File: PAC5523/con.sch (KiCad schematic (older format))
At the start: 38 parts

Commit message: updated schematic
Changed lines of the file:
@@
 Wire Wire Line
 	6950 1450 7050 1450
-Text GLabel 7050 1450 1    50   Input ~ 0
-VIO
 $Comp
 L Device:R_Small R?
@@
 	1    0    0    -1
 $EndComp
+$Comp
+L power:+5V #PWR?
+U 1 1 5D60DF02
+P 7050 1450
+F 0 "#PWR?" H 7050 1300 50  0001 C CNN
+F 1 "+5V" H 7065 1623 50  0000 C CNN
+F 2 "" H 7050 1450 50  0001 C CNN
+F 3 "" H 7050 1450 50  0001 C CNN
+	1    7050 1450
+	1    0    0    -1
+$EndComp
+Connection ~ 7050 1450
 $EndSCHEMATC

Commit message: updated schematic
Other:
- note added: "NTC Spannungsteiler fixen\n"
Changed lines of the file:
@@
 $EndComp
 Connection ~ 7050 1450
+Text Notes 8050 4150 0    50   ~ 0
+NTC Spannungsteiler fixen\n
 $EndSCHEMATC

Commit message: wip
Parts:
- removed J?: CAN, Connector_Molex:Molex_PicoBlade_53261-0371_1x03-1MP_P1.25mm_Horizontal, symbol Connector_Generic_MountingPin:Conn_01x03_MountingPin
- removed JP? (x2): UART/RS485, Jumper:SolderJumper-3_P1.3mm_Bridged2Bar12_Pad1.0x1.5mm, symbol Jumper:Jumper_3_Bridged12
- added J4: GND, otter:PinHeader_1x03_P2.00mm_Vertical_COMBI, symbol Connector:Conn_01x03_Male
- added J5: VIN, otter:PinHeader_1x03_P2.00mm_Vertical_COMBI, symbol Connector:Conn_01x03_Male
- added R43: 100, Resistor_SMD:R_0603_1608Metric, symbol Device:R_Small
- added R44: 1k, Resistor_SMD:R_0603_1608Metric, symbol Device:R_Small
- JP2, JP4: renamed from JP?; footprint Jumper:SolderJumper-3_P1.3mm_Bridged2Bar12_Pad1.0x1.5mm -> Jumper:SolderJumper-3_P1.3mm_Open_Pad1.0x1.5mm_NumberLabels
- gave numbers to parts that had none: 33
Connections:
- net labels added: NTC_EXT, VIN
- wire segments 31 -> 27
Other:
- note removed: "NTC Spannungsteiler fixen\n"
- moved on the sheet: JP2, R32, R39, R4, R5

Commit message: wip
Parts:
- removed JP4: HALL_V, Jumper:SolderJumper-3_P1.3mm_Open_Pad1.0x1.5mm_NumberLabels, symbol Jumper:Jumper_3_Bridged12
- removed R20: 120, Resistor_SMD:R_0603_1608Metric, symbol Device:R_Small
- removed R37: 1k, Resistor_SMD:R_0603_1608Metric, symbol Device:R_Small
- removed R38: 100, Resistor_SMD:R_0603_1608Metric, symbol Device:R_Small
- added J9: LED, Connector_Molex:Molex_PicoBlade_53261-0371_1x03-1MP_P1.25mm_Horizontal, symbol Connector_Generic_MountingPin:Conn_01x03_MountingPin
- added R45: 100, Resistor_SMD:R_0603_1608Metric, symbol Device:R_Small
- added R46, R47: 1k, Resistor_SMD:R_0603_1608Metric, symbol Device:R_Small
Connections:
- net labels added: 3V3, AIN, CANRX, CANTX
- net labels removed: NTC_FET, NTC_FET_PAC, UART_RX, UART_TX
- wire segments 27 -> 35
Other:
- moved on the sheet: R27, R28, R29, R33, R34, R35

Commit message: wip
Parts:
- removed J7: SWD, Connector_PinHeader_2.54mm:PinHeader_1x04_P2.54mm_Vertical, symbol Connector:Conn_01x04_Male
- removed R21, R22: 100, Resistor_SMD:R_0603_1608Metric, symbol Device:R_Small
- added P1: TC2030-CTX-Tag-Connect, otter:TC2030, symbol otter:TC2030-CTX-Tag-Connect
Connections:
- no-connect marks 0 -> 2
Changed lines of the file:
@@
 Wire Wire Line
 	3150 3500 3100 3500
-$Comp
-L Connector:Conn_01x04_Male J?
-U 1 1 5D5B75A0
-P 4900 3450
-AR Path="/5D5B75A0" Ref="J?"  Part="1"
-AR Path="/5D59ABFE/5D5B75A0" Ref="J7"  Part="1"
-F 0 "J7" H 4872 3332 50  0000 R CNN
-F 1 "SWD" H 4872 3423 50  0000 R CNN
-F 2 "Connector_PinHeader_2.54mm:PinHeader_1x04_P2.54mm_Vertical" H 4900 3450 50  0001 C CNN
-F 3 "~" H 4900 3450 50  0001 C CNN
-	1    4900 3450
-	-1   0    0    1
-$EndComp
-Text GLabel 4700 3250 1    50   Input ~ 0
-VIO
-$Comp
-L power:GND #PWR?
-U 1 1 5D5B75A7
-P 4700 3550
-AR Path="/5D5B75A7" Ref="#PWR?"  Part="1"
-AR Path="/5D59ABFE/5D5B75A7" Ref="#PWR0138"  Part="1"
-F 0 "#PWR0138" H 4700 3300 50  0001 C CNN
-F 1 "GND" H 4705 3377 50  0000 C CNN
-F 2 "" H 4700 3550 50  0001 C CNN
-F 3 "" H 4700 3550 50  0001 C CNN
-	1    4700 3550
-	1    0    0    -1
-$EndComp
 Text GLabel 2350 3600 1    50   Input ~ 0
 RS485_A
@@
 	0    1    1    0
 $EndComp
-$Comp
-L Device:R_Small R?
-U 1 1 5D5B75DF
-P 4600 3350
-AR Path="/5D5B75DF" Ref="R?"  Part="1"
-AR Path="/5D59ABFE/5D5B75DF" Ref="R21"  Part="1"
-F 0 "R21" V 4400 3300 50  0000 C CNN
-F 1 "100" V 4500 3300 50  0000 C CNN
-F 2 "Resistor_SMD:R_0603_1608Metric" H 4600 3350 50  0001 C CNN
-F 3 "~" H 4600 3350 50  0001 C CNN
-	1    4600 3350
-	0    1    1    0
-$EndComp
-$Comp
-L Device:R_Small R?
-U 1 1 5D5B75E5
-P 4600 3450
-AR Path="/5D5B75E5" Ref="R?"  Part="1"
-AR Path="/5D59ABFE/5D5B75E5" Ref="R22"  Part="1"
-F 0 "R22" V 4704 3450 50  0000 C CNN
-F 1 "100" V 4795 3450 50  0000 C CNN
-F 2 "Resistor_SMD:R_0603_1608Metric" H 4600 3450 50  0001 C CNN
-F 3 "~" H 4600 3450 50  0001 C CNN
-	1    4600 3450
-	0    1    1    0
-$EndComp
-Text GLabel 4500 3450 0    50   Input ~ 0
-SWDCL
-Text GLabel 4500 3350 0    50   Input ~ 0
-SWDIO
 $Comp
 L power:GND #PWR?
@@
 	5850 3600 6100 3600
 Connection ~ 6100 3600
+$Comp
+L otter:TC2030-CTX-Tag-Connect P?
+U 1 1 5CD67ED4
+P 7800 2500
+AR Path="/5CD67ED4" Ref="P?"  Part="1"
+AR Path="/5D59ABFE/5CD67ED4" Ref="P1"  Part="1"
+F 0 "P1" H 7800 2792 40  0000 C CNN
+F 1 "TC2030-CTX-Tag-Connect" H 7800 2716 40  0000 C CNN
+F 2 "otter:TC2030" H 7800 2500 60  0001 C CNN
+F 3 "" H 7800 2500 60  0001 C CNN
+	1    7800 2500
+	1    0    0    -1
+$EndComp
+Text GLabel 7350 2400 0    50   Input ~ 0
+VIO
+$Comp
+L power:GND #PWR?
+U 1 1 5CD67EDB
+P 7350 2600
+AR Path="/5CD67EDB" Ref="#PWR?"  Part="1"
+AR Path="/5D59ABFE/5CD67EDB" Ref="#PWR0133"  Part="1"
+F 0 "#PWR0133" H 7350 2350 50  0001 C CNN
+F 1 "GND" V 7355 2472 50  0000 R CNN
+F 2 "" H 7350 2600 50  0001 C CNN
+F 3 "" H 7350 2600 50  0001 C CNN
+	1    7350 2600
+	0    1    1    0
+$EndComp
+Text GLabel 8250 2500 2    50   Input ~ 0
+SWDCL
+Text GLabel 8250 2400 2    50   Input ~ 0
+SWDIO
+NoConn ~ 8250 2600
+NoConn ~ 7350 2500
 $EndSCHEMATC

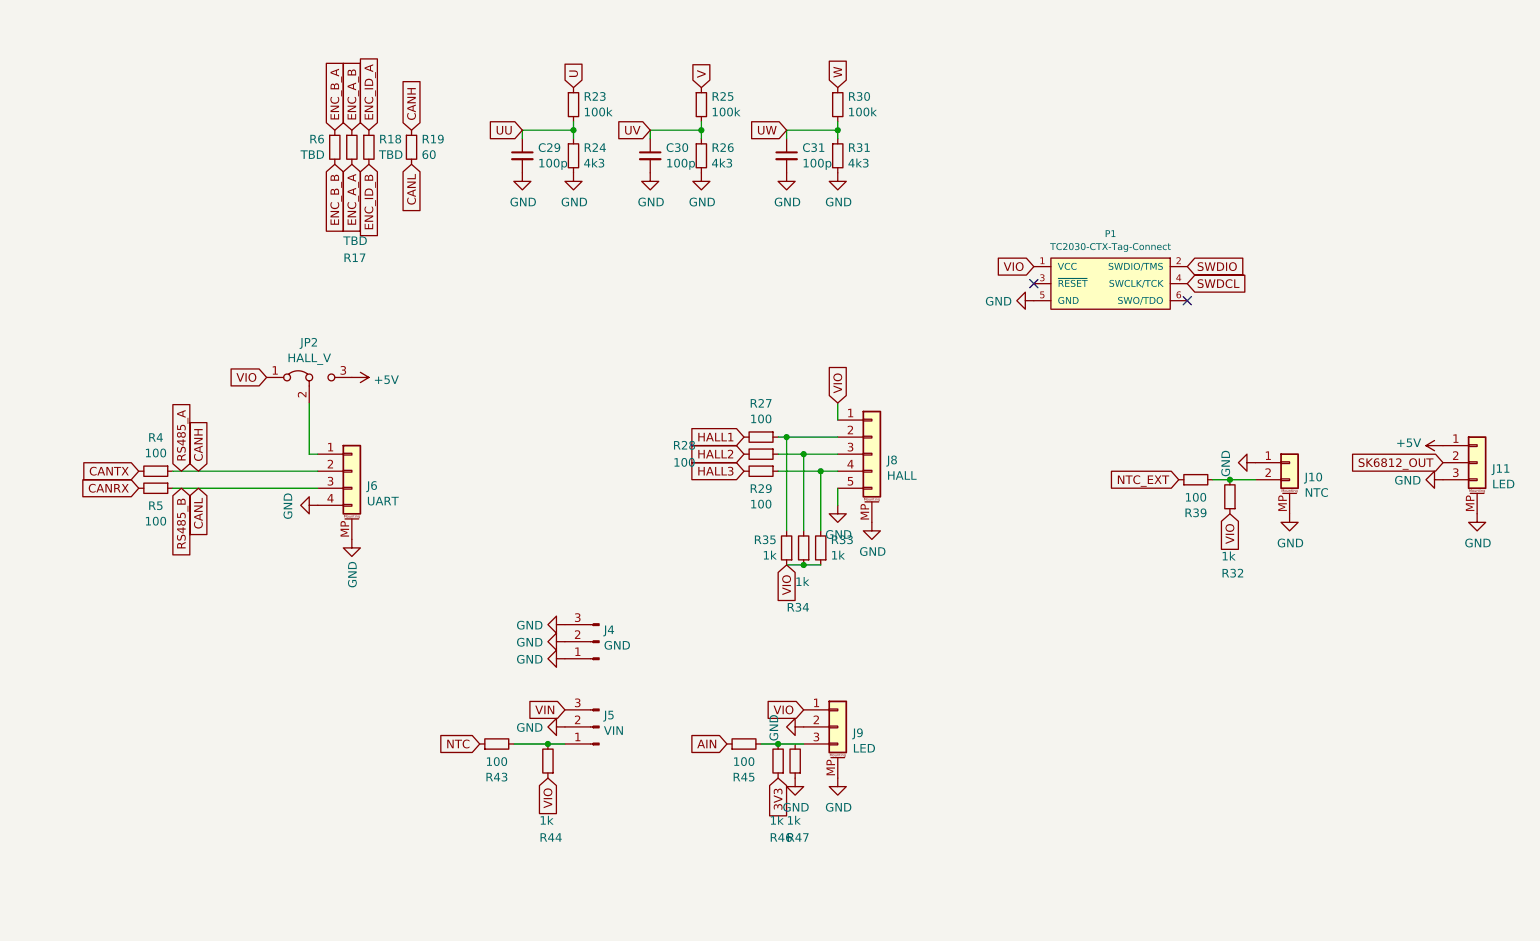
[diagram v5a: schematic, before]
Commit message: added Encoder,LED,NTC
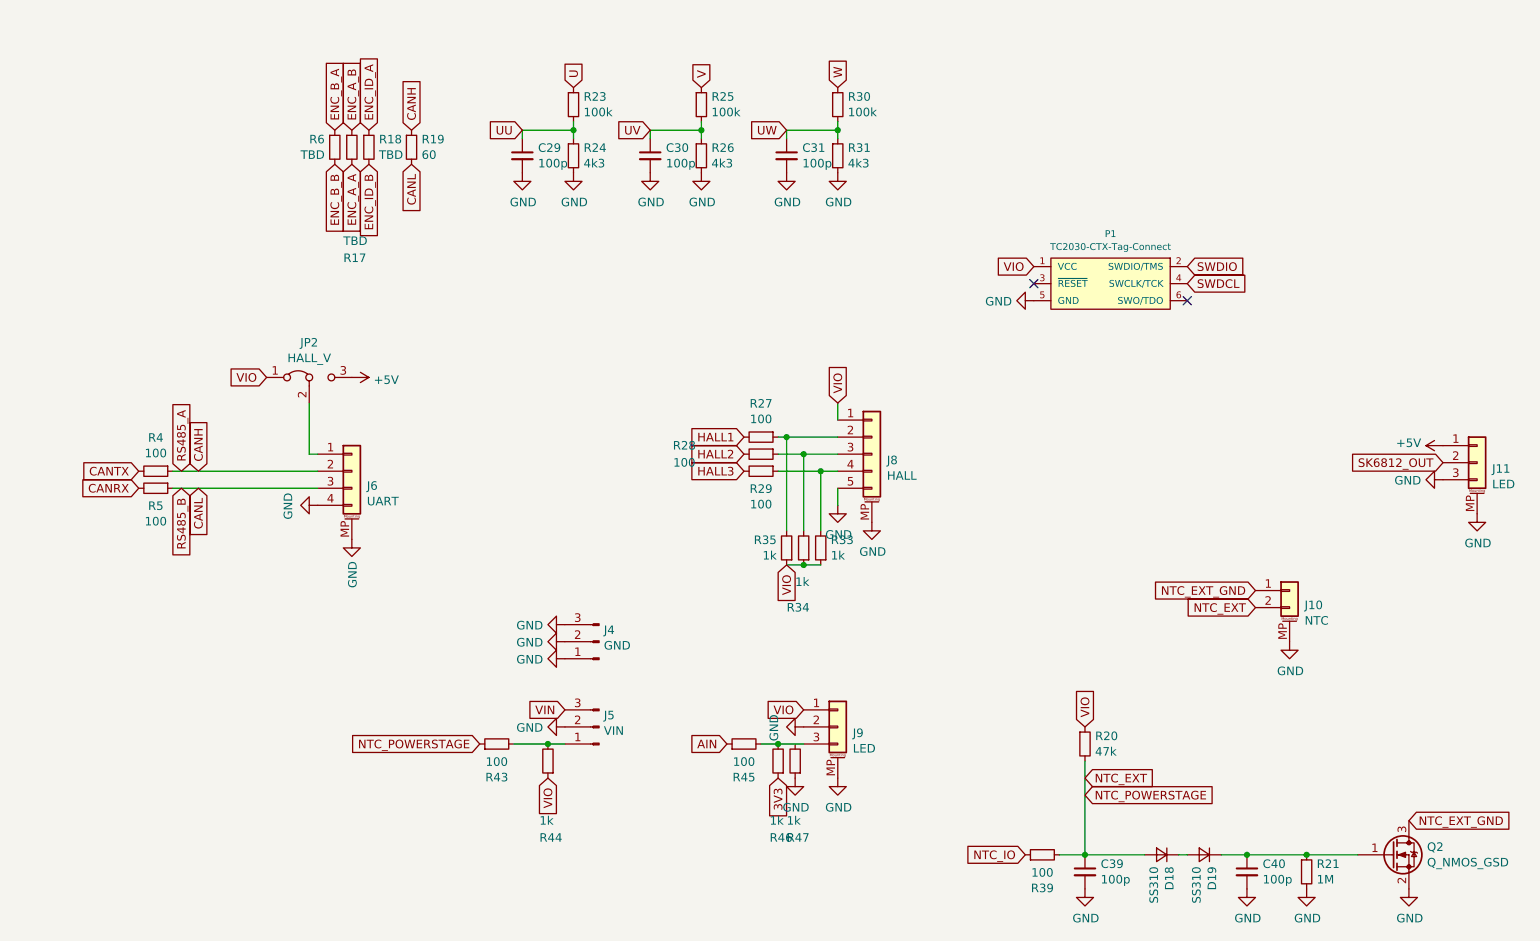
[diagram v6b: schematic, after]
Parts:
- removed R32: 1k, Resistor_SMD:R_0603_1608Metric, symbol Device:R_Small
- added C39, C40: 100p, Capacitor_SMD:C_0603_1608Metric, symbol Device:C_Small
- added D18, D19: SS310, Diode_SMD:D_SOD-123F, symbol Device:D_Small
- added Q2: Q_NMOS_GSD, Package_TO_SOT_SMD:SOT-23, symbol Device:Q_NMOS_GSD
- added R20: 47k, Resistor_SMD:R_0603_1608Metric, symbol Device:R_Small
- added R21: 1M, Resistor_SMD:R_0603_1608Metric, symbol Device:R_Small
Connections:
- net NTC is gone; now on net NTC_EXT: R43.1
- net GND: now also C39.2, C40.2, Q2.2 (S), R21.2; no longer J10.1 (Pin_1)
- net NTC_EXT: now also J10.2 (Pin_2), R39.2, C39.1, D18.2 (A), R20.2; no longer R39.1
- net VIO: now also R20.1
- new net: C40.1, D19.1 (K), Q2.1 (G), R21.1
- new net: D18.1 (K), D19.2 (A)
- new net NTC_EXT_GND: J10.1 (Pin_1), Q2.3 (D)
- new net NTC_IO: R39.1
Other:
- moved on the sheet: J10, R39
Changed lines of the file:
@@
 L Device:R_Small R?
 U 1 1 5D5B7552
-P 8300 3650
+P 7400 5850
 AR Path="/5D5B7552" Ref="R?"  Part="1"
 AR Path="/5D59ABFE/5D5B7552" Ref="R39"  Part="1"
-F 0 "R39" V 8104 3650 50  0000 C CNN
-F 1 "100" V 8195 3650 50  0000 C CNN
-F 2 "Resistor_SMD:R_0603_1608Metric" H 8300 3650 50  0001 C CNN
-F 3 "~" H 8300 3650 50  0001 C CNN
-	1    8300 3650
+F 0 "R39" V 7204 5850 50  0000 C CNN
+F 1 "100" V 7295 5850 50  0000 C CNN
+F 2 "Resistor_SMD:R_0603_1608Metric" H 7400 5850 50  0001 C CNN
+F 3 "~" H 7400 5850 50  0001 C CNN
+	1    7400 5850
 	0    -1   -1   0
 $EndComp
-Text GLabel 8200 3650 0    50   Input ~ 0
+Text GLabel 8650 4400 0    50   Input ~ 0
 NTC_EXT
 Text GLabel 2450 3700 3    50   Input ~ 0
@@
 L Connector_Generic_MountingPin:Conn_01x02_MountingPin J?
 U 1 1 5D5B75FF
-P 8850 3550
+P 8850 4300
 AR Path="/5D5B75FF" Ref="J?"  Part="1"
 AR Path="/5D59ABFE/5D5B75FF" Ref="J10"  Part="1"
-F 0 "J10" H 8938 3464 50  0000 L CNN
-F 1 "NTC" H 8938 3373 50  0000 L CNN
-F 2 "Connector_Molex:Molex_PicoBlade_53261-0271_1x02-1MP_P1.25mm_Horizontal" H 8850 3550 50  0001 C CNN
-F 3 "~" H 8850 3550 50  0001 C CNN
-	1    8850 3550
+F 0 "J10" H 8938 4214 50  0000 L CNN
+F 1 "NTC" H 8938 4123 50  0000 L CNN
+F 2 "Connector_Molex:Molex_PicoBlade_53261-0271_1x02-1MP_P1.25mm_Horizontal" H 8850 4300 50  0001 C CNN
+F 3 "~" H 8850 4300 50  0001 C CNN
+	1    8850 4300
 	1    0    0    -1
 $EndComp
@@
 L power:GND #PWR?
 U 1 1 5D5B7605
-P 8850 3850
+P 8850 4600
 AR Path="/5D5B7605" Ref="#PWR?"  Part="1"
 AR Path="/5D59ABFE/5D5B7605" Ref="#PWR0143"  Part="1"
-F 0 "#PWR0143" H 8850 3600 50  0001 C CNN
-F 1 "GND" H 8855 3677 50  0000 C CNN
-F 2 "" H 8850 3850 50  0001 C CNN
-F 3 "" H 8850 3850 50  0001 C CNN
-	1    8850 3850
-	1    0    0    -1
-$EndComp
-$Comp
-L power:GND #PWR?
-U 1 1 5D5B760B
-P 8650 3550
-AR Path="/5D5B760B" Ref="#PWR?"  Part="1"
-AR Path="/5D59ABFE/5D5B760B" Ref="#PWR0145"  Part="1"
-F 0 "#PWR0145" H 8650 3300 50  0001 C CNN
-F 1 "GND" H 8655 3377 50  0000 C CNN
-F 2 "" H 8650 3550 50  0001 C CNN
-F 3 "" H 8650 3550 50  0001 C CNN
-	1    8650 3550
-	0    1    1    0
+F 0 "#PWR0143" H 8850 4350 50  0001 C CNN
+F 1 "GND" H 8855 4427 50  0000 C CNN
+F 2 "" H 8850 4600 50  0001 C CNN
+F 3 "" H 8850 4600 50  0001 C CNN
+	1    8850 4600
+	1    0    0    -1
 $EndComp
 $Comp
@@
 $EndComp
 Text GLabel 4100 5200 0    50   Input ~ 0
-NTC
+NTC_POWERSTAGE
 Wire Wire Line
 	4300 5200 4500 5200
@@
 	-1   0    0    1
 $EndComp
-Text GLabel 8500 3850 3    50   Input ~ 0
-VIO
-$Comp
-L Device:R_Small R?
-U 1 1 5D5B7514
-P 8500 3750
-AR Path="/5D5B7514" Ref="R?"  Part="1"
-AR Path="/5D59ABFE/5D5B7514" Ref="R32"  Part="1"
-F 0 "R32" H 8550 4200 50  0000 R CNN
-F 1 "1k" H 8550 4100 50  0000 R CNN
-F 2 "Resistor_SMD:R_0603_1608Metric" H 8500 3750 50  0001 C CNN
-F 3 "~" H 8500 3750 50  0001 C CNN
-	1    8500 3750
-	-1   0    0    1
-$EndComp
 Connection ~ 4500 5200
 Wire Wire Line
 	4500 5200 4600 5200
-Wire Wire Line
-	8400 3650 8500 3650
-Connection ~ 8500 3650
-Wire Wire Line
-	8500 3650 8650 3650
 $Comp
 L Device:R_Small R?
@@
 NoConn ~ 8250 2600
 NoConn ~ 7350 2500
+Text GLabel 7650 5400 2    50   Input ~ 0
+NTC_EXT
+Text GLabel 7650 5500 2    50   Input ~ 0
+NTC_POWERSTAGE
+Text GLabel 7300 5850 0    50   Input ~ 0
+NTC_IO
+$Comp
+L Device:R_Small R?
+U 1 1 5CDE0535
+P 8950 5950
+AR Path="/5CDE0535" Ref="R?"  Part="1"
+AR Path="/5D59ABFE/5CDE0535" Ref="R21"  Part="1"
+F 0 "R21" H 9009 5996 50  0000 L CNN
+F 1 "1M" H 9009 5905 50  0000 L CNN
+F 2 "Resistor_SMD:R_0603_1608Metric" H 8950 5950 50  0001 C CNN
+F 3 "~" H 8950 5950 50  0001 C CNN
+	1    8950 5950
+	1    0    0    -1
+$EndComp
+$Comp
+L Device:C_Small C?
+U 1 1 5CDE053B
+P 7650 5950
+AR Path="/5CDE053B" Ref="C?"  Part="1"
+AR Path="/5D59ABFE/5CDE053B" Ref="C39"  Part="1"
+F 0 "C39" H 7742 5996 50  0000 L CNN
+F 1 "100p" H 7742 5905 50  0000 L CNN
+F 2 "Capacitor_SMD:C_0603_1608Metric" H 7650 5950 50  0001 C CNN
+F 3 "~" H 7650 5950 50  0001 C CNN
+	1    7650 5950
+	1    0    0    -1
+$EndComp
+$Comp
+L Device:D_Small D?
+U 1 1 5CDE1DA1
+P 8100 5850
+AR Path="/5CDE1DA1" Ref="D?"  Part="1"
+AR Path="/5D59ABFE/5CDE1DA1" Ref="D18"  Part="1"
+F 0 "D18" V 8054 5918 50  0000 L CNN
+F 1 "SS310" V 8145 5918 50  0000 L CNN
+F 2 "Diode_SMD:D_SOD-123F" V 8100 5850 50  0001 C CNN
+F 3 "~" V 8100 5850 50  0001 C CNN
+	1    8100 5850
+	-1   0    0    1
+$EndComp
+$Comp
+L Device:D_Small D?
+U 1 1 5CDE236C
+P 8350 5850
+AR Path="/5CDE236C" Ref="D?"  Part="1"
+AR Path="/5D59ABFE/5CDE236C" Ref="D19"  Part="1"
+F 0 "D19" V 8304 5918 50  0000 L CNN
+F 1 "SS310" V 8395 5918 50  0000 L CNN
+F 2 "Diode_SMD:D_SOD-123F" V 8350 5850 50  0001 C CNN
+F 3 "~" V 8350 5850 50  0001 C CNN
+	1    8350 5850
+	-1   0    0    1
+$EndComp
+$Comp
+L Device:C_Small C?
+U 1 1 5CDE366D
+P 8600 5950
+AR Path="/5CDE366D" Ref="C?"  Part="1"
+AR Path="/5D59ABFE/5CDE366D" Ref="C40"  Part="1"
+F 0 "C40" H 8692 5996 50  0000 L CNN
+F 1 "100p" H 8692 5905 50  0000 L CNN
+F 2 "Capacitor_SMD:C_0603_1608Metric" H 8600 5950 50  0001 C CNN
+F 3 "~" H 8600 5950 50  0001 C CNN
+	1    8600 5950
+	1    0    0    -1
+$EndComp
+Wire Wire Line
+	8000 5850 7650 5850
+Connection ~ 7650 5850
+Wire Wire Line
+	7650 5850 7500 5850
+Wire Wire Line
+	8950 5850 8600 5850
+Connection ~ 8600 5850
+Wire Wire Line
+	8600 5850 8450 5850
+Wire Wire Line
+	8250 5850 8200 5850
+$Comp
+L power:GND #PWR?
+U 1 1 5CDE791A
+P 8600 6050
+AR Path="/5CDE791A" Ref="#PWR?"  Part="1"
+AR Path="/5D59ABFE/5CDE791A" Ref="#PWR0138"  Part="1"
+F 0 "#PWR0138" H 8600 5800 50  0001 C CNN
+F 1 "GND" H 8605 5877 50  0000 C CNN
+F 2 "" H 8600 6050 50  0001 C CNN
+F 3 "" H 8600 6050 50  0001 C CNN
+	1    8600 6050
+	1    0    0    -1
+$EndComp
+$Comp
+L power:GND #PWR?
+U 1 1 5CDE80DA
+P 8950 6050
+AR Path="/5CDE80DA" Ref="#PWR?"  Part="1"
+AR Path="/5D59ABFE/5CDE80DA" Ref="#PWR0145"  Part="1"
+F 0 "#PWR0145" H 8950 5800 50  0001 C CNN
+F 1 "GND" H 8955 5877 50  0000 C CNN
+F 2 "" H 8950 6050 50  0001 C CNN
+F 3 "" H 8950 6050 50  0001 C CNN
+	1    8950 6050
+	1    0    0    -1
+$EndComp
+$Comp
+L power:GND #PWR?
+U 1 1 5CDE8848
+P 7650 6050
+AR Path="/5CDE8848" Ref="#PWR?"  Part="1"
+AR Path="/5D59ABFE/5CDE8848" Ref="#PWR0158"  Part="1"
+F 0 "#PWR0158" H 7650 5800 50  0001 C CNN
+F 1 "GND" H 7655 5877 50  0000 C CNN
+F 2 "" H 7650 6050 50  0001 C CNN
+F 3 "" H 7650 6050 50  0001 C CNN
+	1    7650 6050
+	1    0    0    -1
+$EndComp
+Wire Wire Line
+	8950 5850 9250 5850
+Connection ~ 8950 5850
+$Comp
+L Device:Q_NMOS_GSD Q2
+U 1 1 5CDECFF4
+P 9450 5850
+F 0 "Q2" H 9656 5896 50  0000 L CNN
+F 1 "Q_NMOS_GSD" H 9656 5805 50  0000 L CNN
+F 2 "Package_TO_SOT_SMD:SOT-23" H 9650 5950 50  0001 C CNN
+F 3 "~" H 9450 5850 50  0001 C CNN
+	1    9450 5850
+	1    0    0    -1
+$EndComp
+$Comp
+L power:GND #PWR0181
+U 1 1 5CDEE814
+P 9550 6050
+F 0 "#PWR0181" H 9550 5800 50  0001 C CNN
+F 1 "GND" H 9555 5877 50  0000 C CNN
+F 2 "" H 9550 6050 50  0001 C CNN
+F 3 "" H 9550 6050 50  0001 C CNN
+	1    9550 6050
+	1    0    0    -1
+$EndComp
+$Comp
+L Device:R_Small R?
+U 1 1 5CDEF71D
+P 7650 5200
+AR Path="/5CDEF71D" Ref="R?"  Part="1"
+AR Path="/5D59ABFE/5CDEF71D" Ref="R20"  Part="1"
+F 0 "R20" H 7709 5246 50  0000 L CNN
+F 1 "47k" H 7709 5155 50  0000 L CNN
+F 2 "Resistor_SMD:R_0603_1608Metric" H 7650 5200 50  0001 C CNN
+F 3 "~" H 7650 5200 50  0001 C CNN
+	1    7650 5200
+	1    0    0    -1
+$EndComp
+Text GLabel 7650 5100 1    50   Input ~ 0
+VIO
+Text GLabel 9550 5650 2    50   Input ~ 0
+NTC_EXT_GND
+Text GLabel 8650 4300 0    50   Input ~ 0
+NTC_EXT_GND
+Wire Wire Line
+	7650 5300 7650 5850
 $EndSCHEMATC

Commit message: placement almost done
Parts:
- removed D18: SS310, Diode_SMD:D_SOD-123F, symbol Device:D_Small
- removed R17, R18, R6: TBD, Resistor_SMD:R_0603_1608Metric, symbol Device:R_Small
- removed R43: 100, Resistor_SMD:R_0603_1608Metric, symbol Device:R_Small
- removed R44, R47: 1k, Resistor_SMD:R_0603_1608Metric, symbol Device:R_Small
- added J7: ENCODER, Connector_Molex:Molex_PicoBlade_53261-0671_1x06-1MP_P1.25mm_Horizontal, symbol Connector_Generic_MountingPin:Conn_01x06_MountingPin
- J9: value LED -> AIN
- JP2: value HALL_V -> UART
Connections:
- net +5V: now also J8.1 (Pin_1), J7.1 (Pin_1)
- net 3V3: now also R20.1; no longer R46.1
- net ENC_A_A: now also J7.2 (Pin_2)
- net ENC_A_B: now also J7.3 (Pin_3)
- net ENC_B_A: now also J7.4 (Pin_4)
- net ENC_B_B: now also J7.5 (Pin_5)
- net GND: now also J9.3 (Pin_3), J7.6 (Pin_6), J7.MP (MountPin); no longer J9.2 (Pin_2)
- net NTC_EXT: now also D19.2 (A), J5.1 (Pin_1)
- net VIO: now also R46.1; no longer J8.1 (Pin_1), R20.1
- net at R45.2, R46.2: now also J9.2 (Pin_2); no longer J9.3 (Pin_3)
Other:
- moved on the sheet: C39, J10, J6, J8, J9, JP2, R20, R27, R28, R29, R33, R34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

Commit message: routing 60% done
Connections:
- net AIN renamed Ain
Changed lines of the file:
@@
 $EndComp
 Text GLabel 7250 3550 0    50   Input ~ 0
-AIN
+Ain
 $Comp
 L power:GND #PWR?
@@
 $EndComp
 Text GLabel 4700 3000 0    50   Input ~ 0
-VIO
-Text GLabel 6250 4300 3    50   Input ~ 0
 VIO
 Wire Wire Line
@@
 Text GLabel 7550 3750 3    50   Input ~ 0
 VIO
+Text GLabel 6250 4300 3    50   Input ~ 0
+VIO
 $EndSCHEMATC
